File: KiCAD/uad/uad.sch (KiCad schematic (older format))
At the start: 32 parts

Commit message: трассировка
не расставлены резисторы/конденсатор емкостных кнопок
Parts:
- removed C? (x2): 12пФ(0603), N_RLC:Конденсатор_SMD_0603, symbol elements:Конденсатор_керамический
- removed C?: 4.7мкФ(1210), N_RLC:Конденсатор_SMD_0603, symbol elements:Конденсатор_керамический
- removed C?: 4.7мкФ(1210), symbol elements:Конденсатор_керамический
- removed DD?: 5559ИНxx(UART-RS485), N_DD:SO-8, symbol elements:5559ИНxx(UART-RS485)
- removed R?: 20 кОм(0805), N_RLC:Резистор_SMD_0805_0,125Вт, symbol elements:Резистор_0,125Вт
- removed ZQ?: Резонатор_кварцевый, N_RLC:Резонатор_РК456МДУ(DIP), symbol elements:Резонатор_кварцевый
- added C9: 4.7мкФ(1210), N_RLC:Конденсатор_SMD_1210, symbol elements:Конденсатор_керамический
- added HL2: Светодиод, N_VD_HL:Светодиод_SMD_0603, symbol elements:Светодиод
- added R11: 100 Ом(0805), N_RLC:Резистор_SMD_0805_0,125Вт, symbol elements:Резистор_0,125Вт
- added VD1: Диод_шоттки, N_VD_HL:Диод_BAR43CFILM_SOT-23, symbol elements:Диод_шоттки
- added XP1, XP2: Вилка_PLS6, N_X:Вилка_PLS6_угловая_вертикальная, symbol elements:Вилка_PLS6
- C10, C11, C12: renamed from C?; footprint (none) -> N_RLC:Конденсатор_SMD_1210
- HL1: renamed from HL?; footprint (none) -> N_VD_HL:Светодиод_SMD_0603
- XP3: renamed from XP?; footprint (none) -> N_X:Вилка_PLD6_угловая_вертикальная
- gave numbers to parts that had none: 20
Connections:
- net labels added: LED_work, NeoPixel_OUT
- net labels removed: SCL, SDA
- wire segments 135 -> 133
- no-connect marks 0 -> 8

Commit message: переделана схема
программирование совмещено с питанием
выход на общую плату - дискретные выхода
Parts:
- removed VD1, VD2: Диод_шоттки, N_VD_HL:Диод_BAR43CFILM_SOT-23, symbol elements:Диод_шоттки
- removed XP1, XP2: Вилка_PLS6, N_X:Вилка_PLS6_угловая_вертикальная, symbol elements:Вилка_PLS6
- removed XP3: Вилка_PLD6_ПРОГ, N_X:Вилка_PLD6_угловая_вертикальная, symbol elements:Вилка_PLD6_ПРОГ
- added XP1: Вилка_PLS8, N_X:Вилка_PLS8_угловая_вертикальная, symbol elements:Вилка_PLS8
- added XP2: Вилка_PLS12, N_X:Вилка_PLS12_угловая_вертикальная, symbol elements:Вилка_PLS12
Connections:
- net labels added: D_Out_1, D_Out_2, D_Out_3, D_Out_4, D_Out_5, D_Out_6, D_Out_7, D_Out_8
- net labels removed: NeoPixel_OUT
- wire segments 133 -> 116
- no-connect marks 8 -> 3

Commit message: проект разбит на листы, лицевая панель расставлена, но не разведена
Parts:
- removed C1, C2, C3, C4, C5, C6, C7, C8: 12пФ(0603), N_RLC:Конденсатор_SMD_0603, symbol elements:Конденсатор_керамический
- removed C10, C11, C12, C9: 4.7мкФ(1210), N_RLC:Конденсатор_SMD_1210, symbol elements:Конденсатор_керамический
- removed DD1: ATmega8A-AU, N_DD:микросхема_ATMEGA-8-161AU, symbol elements:ATmega8A-AU
- removed HL1, HL2: Светодиод, N_VD_HL:Светодиод_SMD_0603, symbol elements:Светодиод
- removed R1, R2, R3, R4, R5, R6, R7, R8: 2 МОм(0805), N_RLC:Резистор_SMD_0805_0,125Вт, symbol elements:Резистор_0,125Вт
- removed R10, R11: 100 Ом(0805), N_RLC:Резистор_SMD_0805_0,125Вт, symbol elements:Резистор_0,125Вт
- removed R9: 20 кОм(0805), N_RLC:Резистор_SMD_0805_0,125Вт, symbol elements:Резистор_0,125Вт
- removed XP1: Вилка_PLS8, N_X:Вилка_PLS8_угловая_вертикальная, symbol elements:Вилка_PLS8
- removed XP2: Вилка_PLS12, N_X:Вилка_PLS12_угловая_вертикальная, symbol elements:Вилка_PLS12
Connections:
- net labels removed: BUT_0_CUP, BUT_0_IN, BUT_1_CUP, BUT_1_IN, BUT_2_CUP, BUT_2_IN, BUT_3_CUP, BUT_3_IN, BUT_4_CUP, BUT_4_IN, BUT_5_CUP, BUT_5_IN, BUT_6_CUP, BUT_6_IN, BUT_7_CUP, BUT_7_IN, BUT_COM_OUT, D_Out_1, D_Out_2, D_Out_3, D_Out_4, D_Out_5, D_Out_6, D_Out_7, D_Out_8, GND, LED_work, MISO, MOSI, PWM_OUT_1, PWM_OUT_2, RES, RX, SCK, TX, VCC
- wire segments 116 -> 0
- no-connect marks 3 -> 0

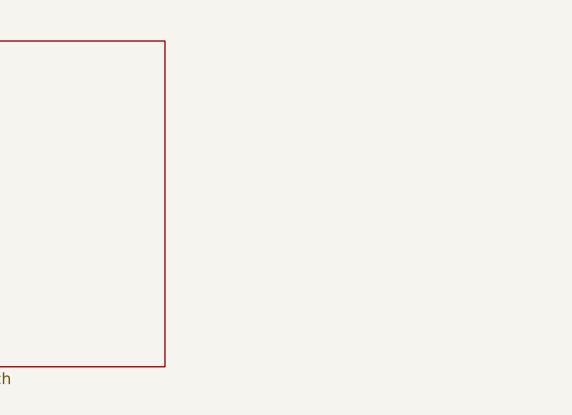
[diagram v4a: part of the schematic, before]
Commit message: в общий проект добавлена лицевая панель под потенциометр
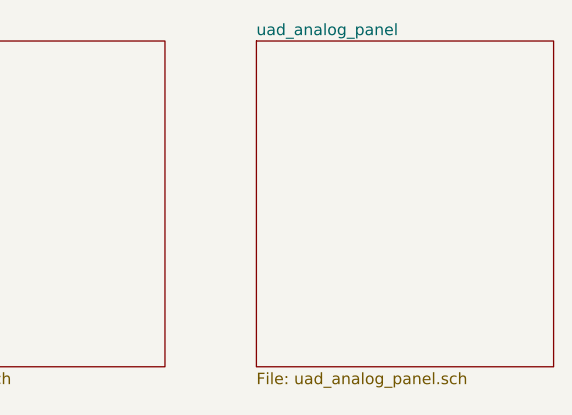
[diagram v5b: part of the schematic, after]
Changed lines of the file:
@@
 $Descr A4 11693 8268
 encoding utf-8
-Sheet 1 3
+Sheet 1 4
 Title ""
 Date ""
@@
 F1 "uab_logic.sch" 50
 $EndSheet
+$Sheet
+S 5150 2300 1300 1425
+U 5C2D1681
+F0 "uad_analog_panel" 50
+F1 "uad_analog_panel.sch" 50
+$EndSheet
 $EndSCHEMATC
